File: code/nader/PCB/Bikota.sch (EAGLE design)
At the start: 6 parts

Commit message: Updated schematic and board files.
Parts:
- added C1: (no value), rcl:C-USC0805
- added FUSE: MF-SMDF050, fuse:MF-SMDF050
- added JP1: Power, pinhead:PINHD-1X2
- added JP2, JP3: (no value), pinhead:PINHD-1X20
- added JP4, JP5, JP6, JP7: (no value), pinhead:PINHD-1X1
- added LED1: (no value), led:LEDCHIPLED_0805
- added Q1: IRLML6244, bytewerk:IRLML6244
- added R1: 100, rcl:R-US_R0805
- added R2, R7: 500, rcl:R-US_R0805
- added R3, R5, R6: 100K, rcl:R-US_R0805
- added R4: 1K, rcl:R-US_R0805
- added SG1: F/CM12P, buzzer:F/CM12P
- added U$7: EPAPERDISPLAY2.9, Bikota:EPAPERDISPLAY2.9
- added U$8: U1V11F5, Bikota:U1V11F5
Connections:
- removed net ESP32_5V: U$1.ESP_5V, U$2.VIN
- new net BUZZER: JP3.15, SG1.2, U$1.2
- new net ESP3V3: JP2.20, R1.1, U$1.ESP_3V3, U$4.VIN
- new net ESP5V: JP2.2, LED1.A, U$1.ESP_5V, U$2.VIN, U$3.VIN, U$5.VIN, U$6.VIN, U$8.VOUT
- new net MOSFET: JP2.8, R2.1, U$1.12
- new net MOSFET_GND: Q1.D, R4.1, U$3.GND, U$4.GND, U$5.GND, U$6.GND
- new net N$11: JP2.6, U$1.13
- new net N$14: JP2.3, U$1.CMD
- new net N$15: JP2.1, U$1.SPK+
- new net N$16: JP4.1, U$1.SPK-
- new net N$17: JP6.1, R7.2
- new net N$18: JP3.2, U$1.23
- new net N$2: R1.2, SG1.1
- new net N$20: JP3.4, U$1.TXD
- new net N$21: JP3.5, U$1.RXD
- new net N$23: JP3.10, U$1.5
- new net N$24: JP3.11, U$1.NC3
- new net N$25: JP3.12, U$1.NC2
- new net N$26: JP3.13, U$1.4
- new net N$27: JP3.14, U$1.0
- new net N$28: JP3.16, U$1.15
- new net N$29: JP3.17, U$1.SD1
- new net N$3: JP2.19, U$1.NC
- new net N$30: JP3.18, U$1.SD0
- new net N$31: JP3.19, U$1.CLK
- new net N$32: JP3.20, U$1.MIC-
- new net N$33: JP5.1, U$1.MIC+
- new net N$412: U$7.VCC
- new net N$413: U$7.GND
- new net N$414: U$7.DIN
- new net N$415: U$7.CLK
- new net N$416: U$7.CS
- new net N$417: U$7.DC
- new net N$418: U$7.RST
- new net N$419: U$7.BUSY
- new net N$5: JP2.14, U$1.32
- new net N$6: LED1.C, R4.2
- new net SVN: C1.1, JP2.17, R5.1, R6.2, U$1.SVN
- new net VBAT+: JP1.1, R5.2, U$8.VIN
- net ACC_INT: now also JP2.9
- net GND: now also C1.2, JP1.2, JP2.7, JP3.1, JP3.7, Q1.S, R3.2, R6.1, R7.1, U$1.GND@2, U$1.GND@3, U$8.GND
- net GPS_TX: now also JP2.15
- net N$1: now also JP2.16, U$1.34; no longer U$3.VIN
- net N$10: now also JP2.10, U$1.27; no longer U$4.VIN
- net N$12: now also JP2.5, U$1.SD2; no longer U$5.GND
- net N$13: now also JP2.4, U$1.SD3; no longer U$5.VIN
- net N$4: now also Q1.G, R2.2, R3.1; no longer U$3.GND
- net N$7: now also JP2.13, U$1.33; no longer U$6.GND
- net N$8: now also JP2.12, U$1.25; no longer U$6.VIN
- net N$9: now also JP2.11, U$1.26; no longer U$4.GND
- net PM10: now also JP3.9
- net PM25: now also JP3.8
- net SCL: now also JP3.3
- net SDA: now also JP3.6
- net SVP: now also JP2.18
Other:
- note added: "via fläche"
- moved on the sheet: U$1, U$2, U$3, U$4, U$5, U$6

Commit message: Update PCB and SCH
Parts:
- removed FUSE: MF-SMDF050, fuse:MF-SMDF050
- added F1: 1206L, ptc-littlefuse:1206L
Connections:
- removed net N$1: JP2.16, U$1.34
- removed net N$28: JP3.16, U$1.15
- removed net N$412: U$7.VCC
- removed net N$413: U$7.GND
- removed net N$414: U$7.DIN
- removed net N$415: U$7.CLK
- removed net N$416: U$7.CS
- removed net N$417: U$7.DC
- removed net N$419: U$7.BUSY
- removed net N$5: JP2.14, U$1.32
- removed net N$7: JP2.13, U$1.33
- removed net N$8: JP2.12, U$1.25
- new net EP_BUSY: JP2.16, U$1.34, U$7.BUSY
- new net EP_CLK: JP2.12, U$1.25, U$7.CLK
- new net EP_CS: JP2.13, U$1.33, U$7.CS
- new net EP_DC: JP2.14, U$1.32, U$7.DC
- new net EP_DIN: JP3.16, U$1.15, U$7.DIN
- new net N$41: F1.2, JP1.1
- net ESP3V3: now also U$7.VCC
- net GND: now also JP7.1, U$7.GND
- net VBAT+: now also F1.1; no longer JP1.1
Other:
- moved on the sheet: JP1, JP7

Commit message: Add files via upload
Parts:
- removed JP7: (no value), pinhead:PINHD-1X1
- added C2, C3, C4, C5, C6, C7: 10uF, rcl:C-USC0805
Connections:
- net ESP3V3: now also C4.1, C7.1
- net ESP5V: now also C2.1, C3.1, C5.1, C6.1
- net GND: now also C2.2, C4.2; no longer JP7.1
- net MOSFET_GND: now also C3.2, C5.2, C6.2, C7.2
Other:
- note removed: "via fläche"
- moved on the sheet: JP6, U$4, U$5

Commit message: Upload V0.1 of PCB
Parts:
- added C8: 10uF, rcl:C-USC0805
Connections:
- net ESP5V: now also C8.1
- net GND: now also C8.2
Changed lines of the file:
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@@
 <part name="C6" library="rcl" library_urn="urn:adsk.eagle:library:334" deviceset="C-US" device="C0805" package3d_urn="urn:adsk.eagle:package:23617/2" value="10uF"/>
 <part name="C7" library="rcl" library_urn="urn:adsk.eagle:library:334" deviceset="C-US" device="C0805" package3d_urn="urn:adsk.eagle:package:23617/2" value="10uF"/>
+<part name="C8" library="rcl" library_urn="urn:adsk.eagle:library:334" deviceset="C-US" device="C0805" package3d_urn="urn:adsk.eagle:package:23617/2" value="10uF"/>
 </parts>
 <sheets>
@@
 <attribute name="VALUE" x="-10.16" y="48.26" size="1.778" layer="96"/>
 </instance>
-<instance part="GND4" gate="1" x="86.36" y="5.08" smashed="yes">
-<attribute name="VALUE" x="83.82" y="2.54" size="1.778" layer="96"/>
+<instance part="GND4" gate="1" x="86.36" y="0" smashed="yes">
+<attribute name="VALUE" x="83.82" y="-2.54" size="1.778" layer="96"/>
 </instance>
 <instance part="JP1" gate="G$1" x="27.94" y="5.08" smashed="yes">
@@
 <attribute name="NAME" x="204.216" y="94.615" size="1.778" layer="95"/>
 <attribute name="VALUE" x="204.216" y="89.789" size="1.778" layer="96"/>
+</instance>
+<instance part="C8" gate="G$1" x="73.66" y="15.24" smashed="yes">
+<attribute name="NAME" x="74.676" y="15.875" size="1.778" layer="95"/>
+<attribute name="VALUE" x="74.676" y="11.049" size="1.778" layer="96"/>
 </instance>
 </instances>
@@
 </segment>
 <segment>
-<wire x1="91.44" y1="25.4" x2="55.88" y2="25.4" width="0.1524" layer="91"/>
+<wire x1="91.44" y1="25.4" x2="73.66" y2="25.4" width="0.1524" layer="91"/>
 <label x="68.58" y="25.4" size="1.778" layer="95"/>
 <pinref part="U$1" gate="G$1" pin="ESP_5V"/>
 <pinref part="JP2" gate="A" pin="2"/>
+<pinref part="C8" gate="G$1" pin="1"/>
+<wire x1="73.66" y1="25.4" x2="55.88" y2="25.4" width="0.1524" layer="91"/>
+<wire x1="73.66" y1="25.4" x2="73.66" y2="17.78" width="0.1524" layer="91"/>
+<junction x="73.66" y="25.4"/>
 </segment>
 <segment>
@@
 <net name="GND" class="0">
 <segment>
-<wire x1="91.44" y1="38.1" x2="86.36" y2="38.1" width="0.1524" layer="91"/>
+<pinref part="GND4" gate="1" pin="GND"/>
 <pinref part="U$1" gate="G$1" pin="GND@1"/>
-<wire x1="86.36" y1="38.1" x2="86.36" y2="7.62" width="0.1524" layer="91"/>
-<pinref part="GND4" gate="1" pin="GND"/>
 <pinref part="JP2" gate="A" pin="7"/>
 <wire x1="55.88" y1="38.1" x2="86.36" y2="38.1" width="0.1524" layer="91"/>
+<wire x1="86.36" y1="38.1" x2="91.44" y2="38.1" width="0.1524" layer="91"/>
+<wire x1="86.36" y1="38.1" x2="86.36" y2="7.62" width="0.1524" layer="91"/>
 <junction x="86.36" y="38.1"/>
-</segment>
-<segment>
+<pinref part="C8" gate="G$1" pin="2"/>
+<wire x1="86.36" y1="7.62" x2="86.36" y2="2.54" width="0.1524" layer="91"/>
+<wire x1="73.66" y1="10.16" x2="73.66" y2="7.62" width="0.1524" layer="91"/>
+<wire x1="73.66" y1="7.62" x2="86.36" y2="7.62" width="0.1524" layer="91"/>
+<junction x="86.36" y="7.62"/>
+</segment>
+<segment>

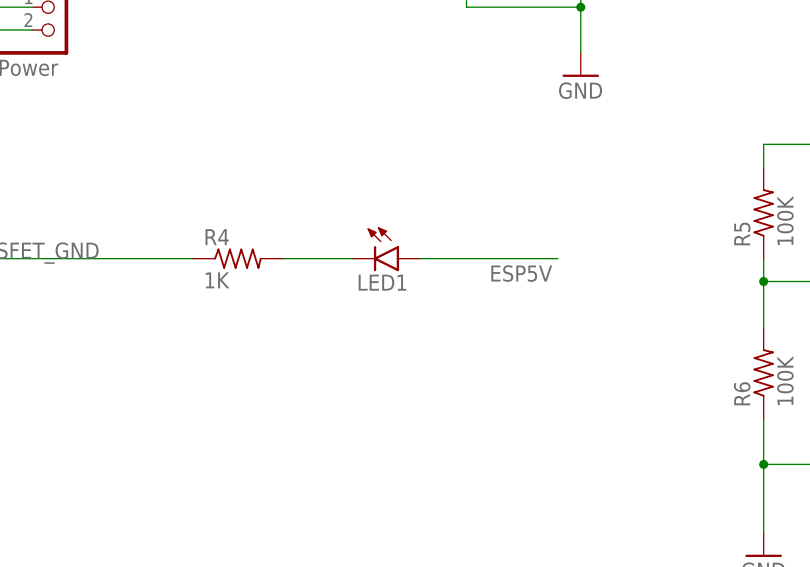
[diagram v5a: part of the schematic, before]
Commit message: Update V0.1
- put "3-5V" below the input socket
- named the mosfet-led "MOSFET" instead of "LED1"
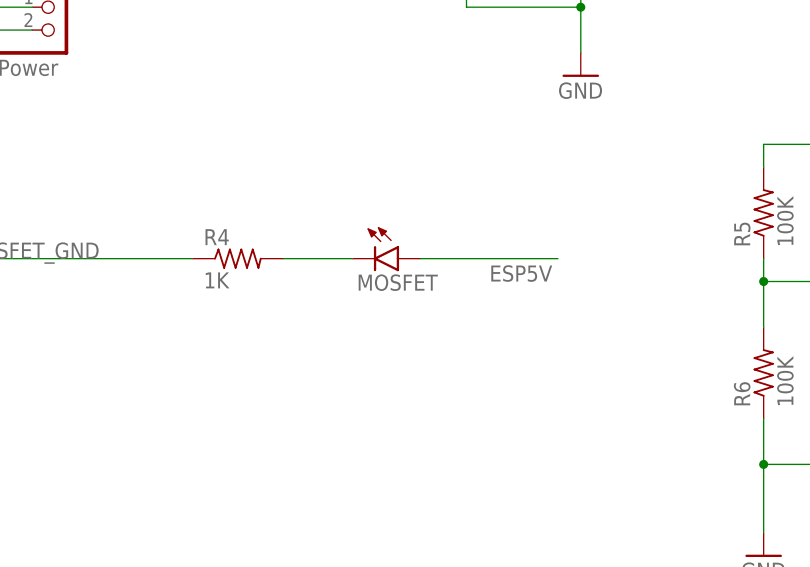
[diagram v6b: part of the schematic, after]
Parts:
- renumbered LED1 to MOSFET
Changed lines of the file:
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@@
 <part name="R3" library="rcl" library_urn="urn:adsk.eagle:library:334" deviceset="R-US_" device="R0805" package3d_urn="urn:adsk.eagle:package:23553/2" value="100K"/>
 <part name="R4" library="rcl" library_urn="urn:adsk.eagle:library:334" deviceset="R-US_" device="R0805" package3d_urn="urn:adsk.eagle:package:23553/2" value="1K"/>
-<part name="LED1" library="led" library_urn="urn:adsk.eagle:library:259" deviceset="LED" device="CHIPLED_0805" package3d_urn="urn:adsk.eagle:package:15821/2"/>
+<part name="MOSFET" library="led" library_urn="urn:adsk.eagle:library:259" deviceset="LED" device="CHIPLED_0805" package3d_urn="urn:adsk.eagle:package:15821/2"/>
 <part name="R5" library="rcl" library_urn="urn:adsk.eagle:library:334" deviceset="R-US_" device="R0805" package3d_urn="urn:adsk.eagle:package:23553/2" value="100K"/>
 <part name="R6" library="rcl" library_urn="urn:adsk.eagle:library:334" deviceset="R-US_" device="R0805" package3d_urn="urn:adsk.eagle:package:23553/2" value="100K"/>
@@
 <attribute name="VALUE" x="44.45" y="-23.622" size="1.778" layer="96"/>
 </instance>
-<instance part="LED1" gate="G$1" x="66.04" y="-20.32" smashed="yes" rot="R270">
+<instance part="MOSFET" gate="G$1" x="66.04" y="-20.32" smashed="yes" rot="R270">
 <attribute name="NAME" x="61.468" y="-23.876" size="1.778" layer="95"/>
 <attribute name="VALUE" x="61.468" y="-26.035" size="1.778" layer="96"/>
@@
 </segment>
 <segment>
-<pinref part="LED1" gate="G$1" pin="A"/>
+<pinref part="MOSFET" gate="G$1" pin="A"/>
 <wire x1="68.58" y1="-20.32" x2="83.82" y2="-20.32" width="0.1524" layer="91"/>
 <label x="76.2" y="-22.86" size="1.778" layer="95"/>
@@
 <segment>
 <pinref part="R4" gate="G$1" pin="2"/>
-<pinref part="LED1" gate="G$1" pin="C"/>
+<pinref part="MOSFET" gate="G$1" pin="C"/>
 <wire x1="53.34" y1="-20.32" x2="60.96" y2="-20.32" width="0.1524" layer="91"/>
 </segment>
